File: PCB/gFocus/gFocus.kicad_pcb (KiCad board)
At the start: 2 copper layers, 44.6 x 44.6 mm, 49 parts, among them J1 FTSH-105-01-F-DV-P-TR, J2 Conn_Coaxial, J3 Conn_02x06_Counter_Clockwise, J4 USB_B_Micro, U1 NMA0515SC, U2 TPS7A3001DGNT, U3 TPS7A4901DGNR, U4 AD5761RBRUZ-RL7, U5 ATSAMD21G18A-A, U6 IP4234CZ6, U8 LDK130-32_SOT23_SOT353

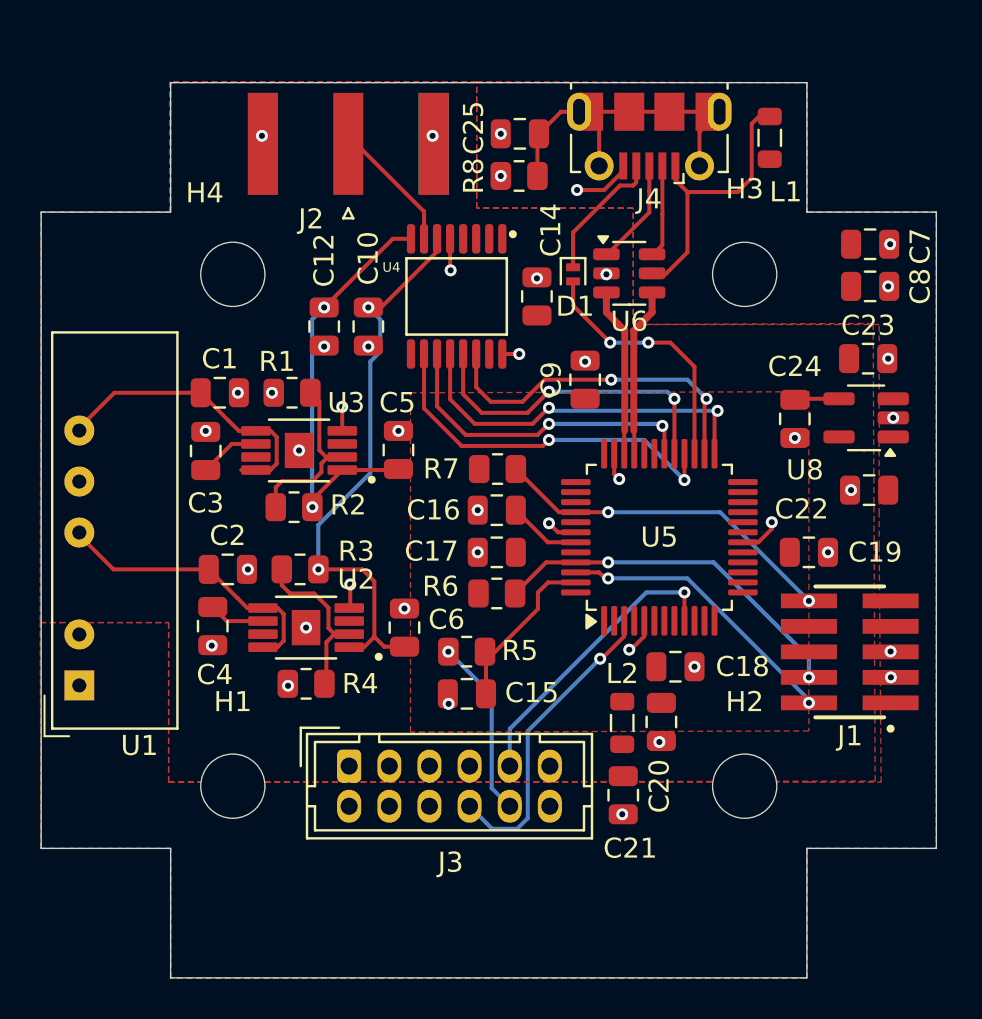
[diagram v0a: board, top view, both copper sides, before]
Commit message: added drivers
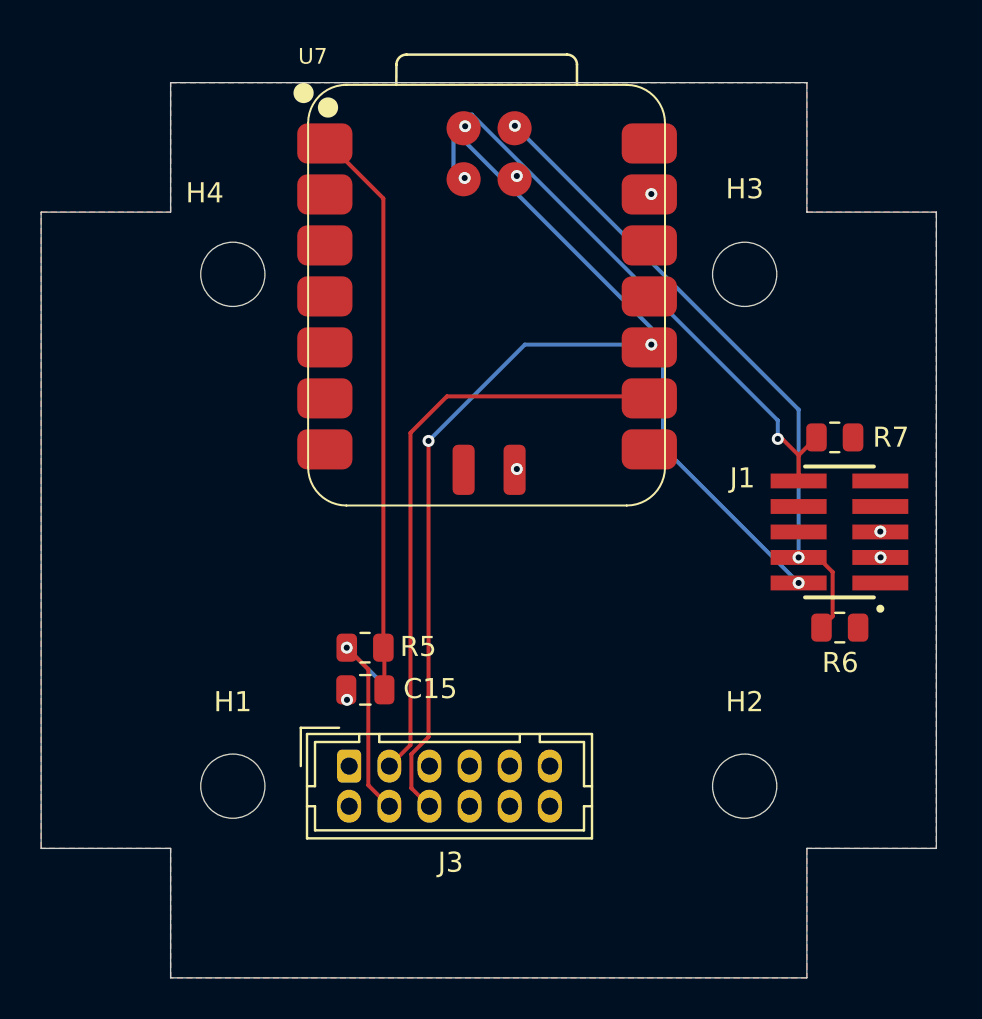
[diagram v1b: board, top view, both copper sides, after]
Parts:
- removed C1, C2, C20, C21, C5, C6, C7: 10u, Capacitor_SMD:C_0805_2012Metric
- removed C10, C12, C14, C17, C18, C19, C8, C9: 100n, Capacitor_SMD:C_0805_2012Metric
- removed C16, C22, C23: 1u, Capacitor_SMD:C_0805_2012Metric
- removed C24, C3, C4: 10n, Capacitor_SMD:C_0805_2012Metric
- removed C25: 4.5n, Capacitor_SMD:C_0805_2012Metric
- removed D1: PMEG2005EL, Diode_SMD:D_SOD-882
- removed J2: Conn_Coaxial, Connector_Coaxial:SMA_Amphenol_132289_EdgeMount
- removed J4: USB_B_Micro, Connector_USB:USB_Micro-B_Molex-105017-0001
- removed L1, L2: 10u, Inductor_SMD:L_0805_2012Metric
- removed R1, R4: 10k, Resistor_SMD:R_0805_2012Metric
- removed R2, R3: 93.1k, Resistor_SMD:R_0805_2012Metric
- removed R8: 1M, Resistor_SMD:R_0805_2012Metric
- removed U1: NMA0515SC, Converter_DCDC:Converter_DCDC_Murata_NMAxxxxSC_THT
- removed U2: TPS7A3001DGNT, TPS7A3001DGNT:SOP65P490X110-9N
- removed U3: TPS7A4901DGNR, TPS7A3001DGNT:SOP65P490X110-9N
- removed U4: AD5761RBRUZ-RL7, AD5761RBRUZ-RL7:SOP65P640X120-16N
- removed U5: ATSAMD21G18A-A, Package_QFP:TQFP-48_7x7mm_P0.5mm
- removed U6: IP4234CZ6, Package_TO_SOT_SMD:SOT-23-6
- removed U8: LDK130-32_SOT23_SOT353, Package_TO_SOT_SMD:SOT-23-5_HandSoldering
- added U7: XIAO-SAMD21-SMD, Seeed Studio XIAO Series Library:XIAO-SAMD21-SMD, F.Cu at (136.9, 96.5)
- moved R6 17.2 mm to (163.4, 102.5), turned to 180 degrees
- moved R7 16.9 mm to (163.1, 93.0), turned to 180 degrees
- moved J1 6.00 mm to (163.4, 97.7)
- moved C15 5.07 mm to (139.8, 105.6)
- moved R5 5.07 mm to (139.7, 103.5)
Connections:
- J1 pad 01: +3.3V -> VDD
- J3 pad 10: Net-(J3-Pin_10) -> unconnected-(J3-Pin_10-Pad10)
- J3 pad 11: unconnected-(J3-Pin_11-Pad11) -> VDD
- J3 pad 12: +5V -> GND
- J3 pad 2: GND -> unconnected-(J3-Pin_2-Pad2)
- J3 pad 3: unconnected-(J3-Pin_3-Pad3) -> S_DIN
- J3 pad 4: unconnected-(J3-Pin_4-Pad4) -> Net-(J3-Pin_4)
- J3 pad 6: unconnected-(J3-Pin_6-Pad6) -> S_CLK
- J3 pad 8: S_CLK -> unconnected-(J3-Pin_8-Pad8)
- J3 pad 9: S_DIN -> unconnected-(J3-Pin_9-Pad9)
- R5 pad 1: Net-(J3-Pin_10) -> Net-(J3-Pin_4)
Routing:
- net -12V: track 28.9 -> 0.00 mm, vias 2 -> 0
- net +12V: track 21.4 -> 0.00 mm, vias 2 -> 0
- net S_OUT: track 9.14 -> 29.1 mm
- net MISO: track 18.7 -> 0.00 mm, vias 2 -> 0
- net MOSI: track 18.7 -> 0.00 mm, vias 2 -> 0
- net CLK: track 17.1 -> 0.00 mm, vias 2 -> 0
- net Net-(J4-Shield): track 17.0 -> 0.00 mm
- net S_CLK: track 15.5 -> 32.1 mm, vias 1 -> 2
- net SYNC: track 16.2 -> 0.00 mm, vias 2 -> 0
- net LDAC: track 16.1 -> 0.00 mm, vias 2 -> 0
- net SWDIO: track 14.4 -> 29.8 mm
- net S_DIN: track 14.8 -> 29.8 mm, vias 1 -> 0
- net +15V: track 14.9 -> 0.00 mm
- net -15V: track 14.5 -> 0.00 mm
- net GND: track 14.5 -> 0.00 mm, vias 43 -> 6
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- removed copper zone on F.Cu, net +3.3V
- removed copper zone on F.Cu, net +5V
